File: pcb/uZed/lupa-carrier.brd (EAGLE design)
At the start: 101.6 x 57.1 mm, 76 parts, among them K1 694108105102

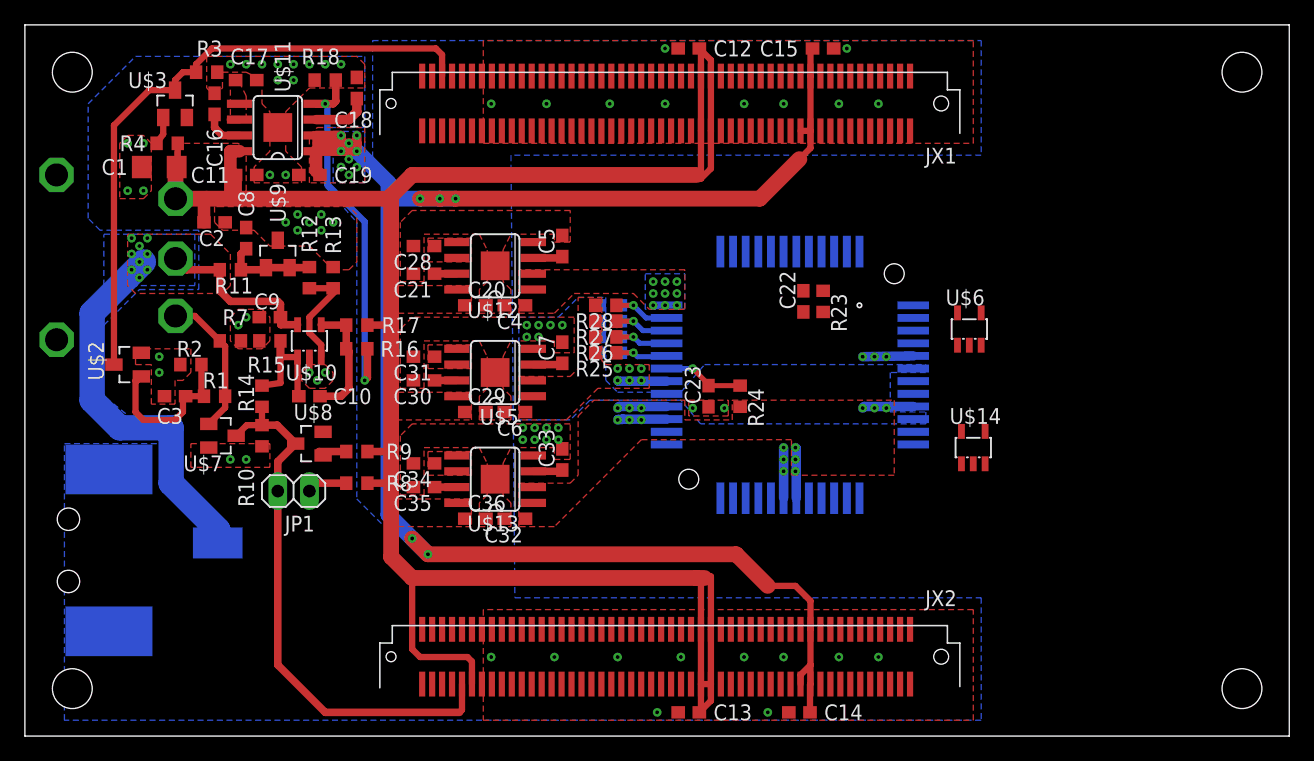
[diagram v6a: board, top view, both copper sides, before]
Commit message: started clock and data pin routing
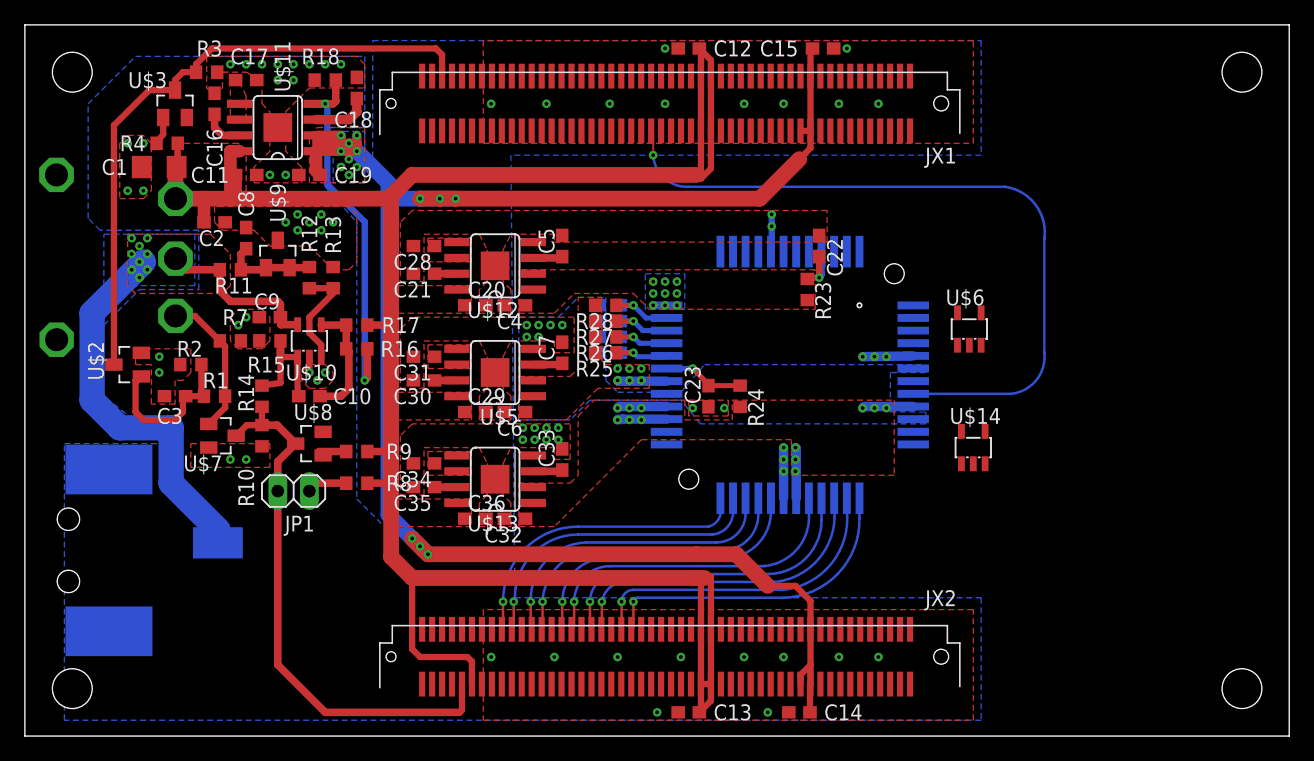
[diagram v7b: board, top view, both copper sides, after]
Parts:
- moved C22 4.62 mm to (63.8, 39.4), turned to 270 degrees
- moved R23 1.59 mm to (62.9, 35.9)
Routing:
- net CLK: track 0.00 -> 57.8 mm, vias 0 -> 1
- net D4: track 0.00 -> 25.5 mm, vias 0 -> 1
- net D3: track 0.00 -> 25.4 mm, vias 0 -> 1
- net D2: track 0.00 -> 25.1 mm, vias 0 -> 1
- net D0: track 0.00 -> 24.9 mm, vias 0 -> 1
- net D1: track 0.00 -> 24.8 mm, vias 0 -> 1
- net D8: track 0.00 -> 24.1 mm, vias 0 -> 1
- net D9: track 0.00 -> 23.8 mm, vias 0 -> 1
- net D7: track 0.00 -> 23.8 mm, vias 0 -> 1
- net D6: track 0.00 -> 23.7 mm, vias 0 -> 1
- net D5: track 0.00 -> 23.1 mm, vias 0 -> 1
- net PRECHARGE_BIAS: track 0.00 -> 4.83 mm, vias 0 -> 1
- net GND_DRIVERS: track 0.00 -> 3.00 mm, vias 0 -> 2
- net VCCIO: vias 14 -> 15

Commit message: more work on power dist
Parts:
- added C37, C38, C39, C40, C41, C42: 1uF, rcl:C0603
- added U$15: XC6210B252MR-G, lupa300-components:SOT25
- moved U$14 6.30 mm to (72.1, 18.4)
- moved U$6 0.63 mm to (75.2, 32.7)
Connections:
- new net VDDD1: C42.1, U$15.5, U$4.P$23
- net 5V: now also C37.1, C39.1, C41.1, U$15.1
- net D0: now also JX2.P$12; no longer JX2.P$58
- net D1: now also JX2.P$14; no longer JX2.P$60
- net D2: now also JX2.P$18; no longer JX2.P$64
- net D3: now also JX2.P$20; no longer JX2.P$66
- net D4: now also JX2.P$26; no longer JX2.P$70
- net D5: now also JX2.P$28; no longer JX2.P$72
- net D6: now also JX2.P$32; no longer JX2.P$76
- net D7: now also JX2.P$34; no longer JX2.P$78
- net D8: now also JX2.P$38; no longer JX2.P$82
- net D9: now also JX2.P$40; no longer JX2.P$84
- net GND: now also C29.2, C30.2, C31.2, C6.2, C7.2, U$4.P$20, U$4.P$3, U$4.P$7, U$5.9
- net GNDA: no longer C29.2, C30.2, C31.2, C6.2, C7.2, U$4.P$20, U$4.P$3, U$4.P$7, U$5.9
- net GNDD: now also C37.2, C38.2, C41.2, C42.2, U$15.2
- net GNDO: now also C39.2, C40.2
- net VDDD: now also C38.1; no longer U$4.P$23
- net VDDD_EN: now also U$15.3
- net VDDO: now also C40.1
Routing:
- net D3: track 25.4 -> 10.7 mm
- net D4: track 25.5 -> 11.1 mm
- net D2: track 25.1 -> 10.7 mm
- net D0: track 24.9 -> 10.6 mm
- net D1: track 24.8 -> 10.6 mm
- net D8: track 24.1 -> 10.6 mm
- net D9: track 23.8 -> 10.6 mm
- net D6: track 23.7 -> 10.6 mm
- net D7: track 23.8 -> 10.8 mm
- net D5: track 23.1 -> 10.9 mm
- net VCCIO: track 141.3 -> 142.8 mm
- net GND: vias 52 -> 71
- added copper zone on layer 1, net GNDD
- added copper zone on layer 16, net GNDD
- added copper zone on layer 1, net GNDO
- added copper zone on layer 16, net GNDO
- added copper zone on layer 1, net VDDD1
- added copper zone on layer 16, net VDDD1
- added copper zone on layer 1, net VDDO
- added copper zone on layer 16, net VDDO
- removed copper zone on layer 1, net GNDA
- removed copper zone on layer 16, net GNDA
